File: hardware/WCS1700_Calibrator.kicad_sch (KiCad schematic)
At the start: 78 parts, among them J1 PJ-002B, J2 560020-0330, J3 282834-8, J4 Conn_01x03_Pin, J5 282834-6, Q1 AO3422, Q2 AO3422, Q3 AO3422, Q4 AO3422, Q5 AO3422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

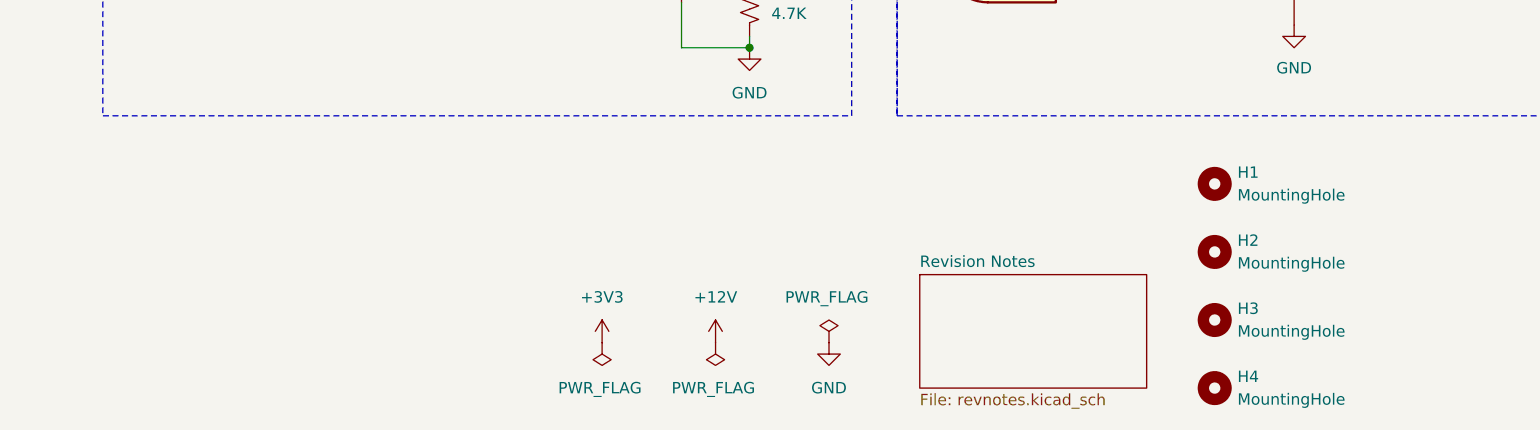
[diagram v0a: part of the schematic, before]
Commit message: Added chassis pour and tied mounting holes to it.
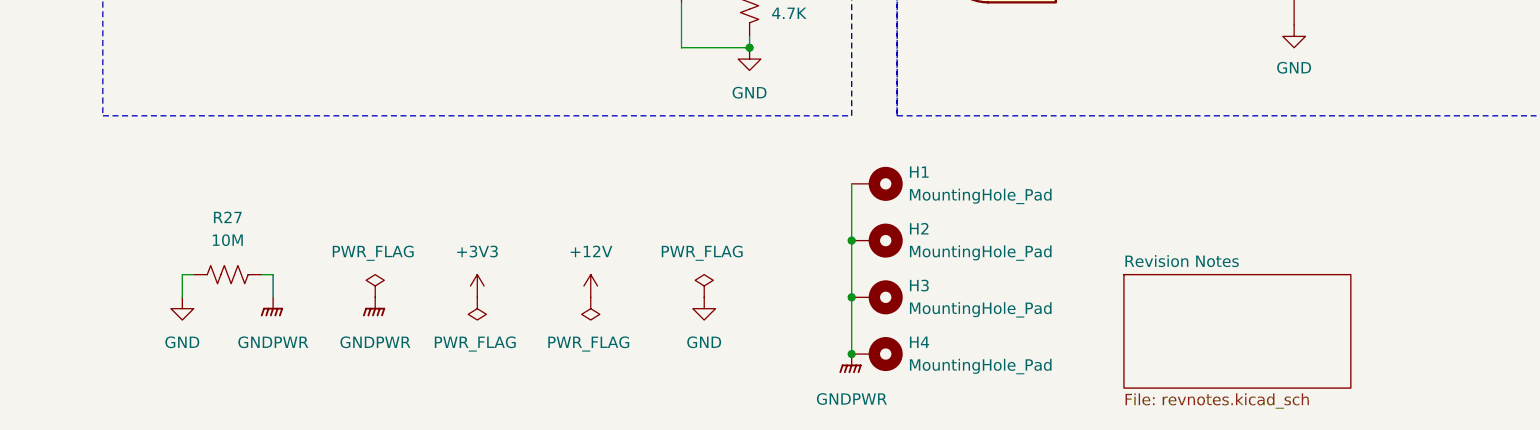
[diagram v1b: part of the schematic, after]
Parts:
- removed H1, H2, H3, H4: MountingHole, MountingHole:MountingHole_4mm_Pad_Via, symbol Mechanical:MountingHole
- added H1, H2, H3, H4: MountingHole_Pad, MountingHole:MountingHole_4mm_Pad_Via, symbol Mechanical:MountingHole_Pad
- added R27: 10M, Resistor_SMD:R_0402_1005Metric_Pad0.72x0.64mm_HandSolder, symbol Device:R_US
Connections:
- net GND: now also R27.1
- new net GNDPWR: H1.1, H2.1, H3.1, H4.1, R27.2

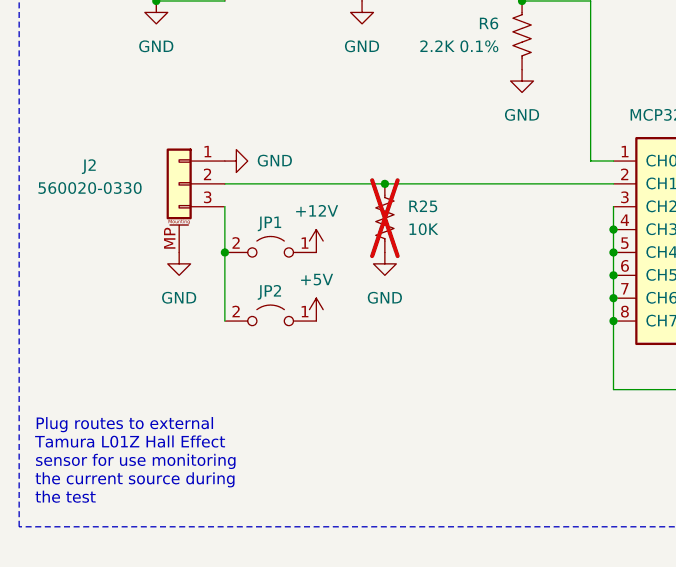
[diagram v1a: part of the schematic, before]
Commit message: Changed jumpers to resistors for L01Z sensor, updated fab/asy docs.
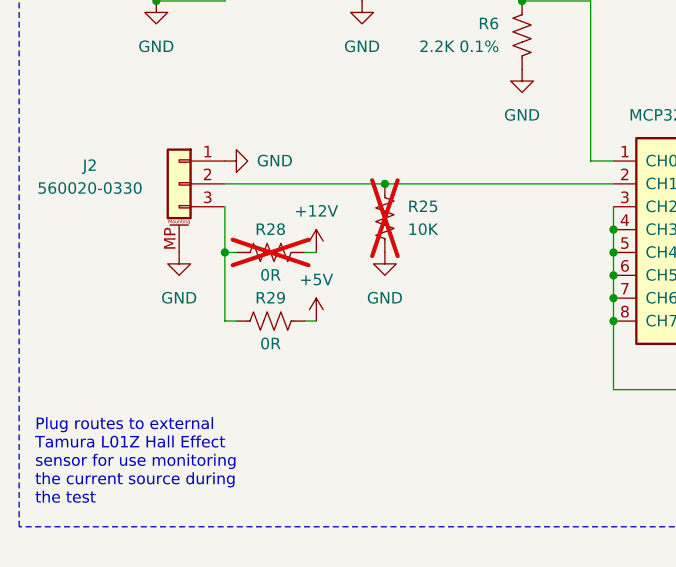
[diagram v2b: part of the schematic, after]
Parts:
- removed JP1, JP2: Jumper_2_Open, Jumper:SolderJumper-2_P1.3mm_Open_TrianglePad1.0x1.5mm, symbol Jumper:Jumper_2_Open
- added R28, R29: 0R, Resistor_SMD:R_1206_3216Metric_Pad1.30x1.75mm_HandSolder, symbol Device:R_US
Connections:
- net +12V: now also R28.2
- net +5V: now also R29.2
- net at J2.3 (Pin_3): now also R28.1, R29.1
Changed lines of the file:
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@@
   (junction (at 111.76 134.62) (diameter 0) (color 0 0 0 0)
   )
+  (junction (at 48.26 170.18) (diameter 0) (color 0 0 0 0)
+  )
   (junction (at 91.44 167.64) (diameter 0) (color 0 0 0 0)
   )
@@
   (junction (at 91.44 177.8) (diameter 0) (color 0 0 0 0)
   )
-  (junction (at 48.26 170.18) (diameter 0) (color 0 0 0 0)
-  )
   (junction (at 66.04 162.56) (diameter 0) (color 0 0 0 0)
   )
@@
     (stroke (width 0) (type default))
   )
-  (wire (pts (xy 48.26 170.18) (xy 48.26 177.8))
-    (stroke (width 0) (type default))
-  )
   (wire (pts (xy 81.28 258.064) (xy 81.28 256.54))
     (stroke (width 0) (type default))
@@
     (stroke (width 0) (type default))
   )
+  (wire (pts (xy 48.26 170.18) (xy 49.53 170.18))
+    (stroke (width 0) (type default))
+  )
   (wire (pts (xy 227.33 232.41) (xy 227.33 231.14))
     (stroke (width 0) (type default))
@@
     (stroke (width 0) (type default))
   )
+  (wire (pts (xy 57.15 170.18) (xy 58.42 170.18))
+    (stroke (width 0) (type default))
+  )
   (wire (pts (xy 351.79 152.4) (xy 355.6 152.4))
     (stroke (width 0) (type default))
@@
     (stroke (width 0) (type dash))
   )
+  (wire (pts (xy 57.15 177.8) (xy 58.42 177.8))
+    (stroke (width 0) (type default))
+  )
   (bus (pts (xy 157.48 58.42) (xy 144.78 58.42))
     (stroke (width 0) (type default))
@@
     (stroke (width 0) (type default))
   )
+  (wire (pts (xy 48.26 170.18) (xy 48.26 177.8))
+    (stroke (width 0) (type default))
+  )
   (wire (pts (xy 200.66 76.2) (xy 233.68 76.2))
     (stroke (width 0) (type default))
@@
     (stroke (width 0) (type default))
   )
+  (wire (pts (xy 48.26 177.8) (xy 49.53 177.8))
+    (stroke (width 0) (type default))
+  )
   (wire (pts (xy 88.9 160.02) (xy 91.44 160.02))
     (stroke (width 0) (type default))
@@
     )
   )
-  (symbol (lib_id "Jumper:Jumper_2_Open") (at 53.34 177.8 0) (mirror y) (unit 1)
-    (in_bom yes) (on_board yes) (dnp no)
-    (property "Reference" "JP2" (at 53.34 174.498 0)
-      (effects (font (size 1.27 1.27)))
-    )
-    (property "Value" "Jumper_2_Open" (at 53.34 173.99 0)
-      (effects (font (size 1.27 1.27)) hide)
-    )
-    (property "Footprint" "Jumper:SolderJumper-2_P1.3mm_Open_TrianglePad1.0x1.5mm" (at 53.34 177.8 0)
-      (effects (font (size 1.27 1.27)) hide)
-    )
-    (property "Datasheet" "~" (at 53.34 177.8 0)
-      (effects (font (size 1.27 1.27)) hide)
-    )
-    (pin "1")
-    (pin "2")
-    (instances
-      (project "WCS1700_Calibrator"
-        (path "/1f03928c-0f24-4718-b1ed-d2ed2f2fbec7"
-          (reference "JP2") (unit 1)
-        )
-      )
-    )
-  )
   (symbol (lib_id "power:+5V") (at 351.79 152.4 0) (unit 1)
     (in_bom yes) (on_board yes) (dnp no) (fields_autoplaced)
@@
     )
   )
-  (symbol (lib_id "Jumper:Jumper_2_Open") (at 53.34 170.18 0) (mirror y) (unit 1)
-    (in_bom yes) (on_board yes) (dnp no)
-    (property "Reference" "JP1" (at 53.34 166.878 0)
-      (effects (font (size 1.27 1.27)))
-    )
-    (property "Value" "Jumper_2_Open" (at 53.34 166.37 0)
-      (effects (font (size 1.27 1.27)) hide)
-    )
-    (property "Footprint" "Jumper:SolderJumper-2_P1.3mm_Open_TrianglePad1.0x1.5mm" (at 53.34 170.18 0)
-      (effects (font (size 1.27 1.27)) hide)
-    )
-    (property "Datasheet" "~" (at 53.34 170.18 0)
-      (effects (font (size 1.27 1.27)) hide)
-    )
-    (pin "1")
-    (pin "2")
-    (instances
-      (project "WCS1700_Calibrator"
-        (path "/1f03928c-0f24-4718-b1ed-d2ed2f2fbec7"
-          (reference "JP1") (unit 1)
-        )
-      )
-    )
-  )
   (symbol (lib_id "power:+5V") (at 215.9 190.5 0) (mirror y) (unit 1)
     (in_bom yes) (on_board yes) (dnp no) (fields_autoplaced)
@@
     )
   )
+  (symbol (lib_id "Device:R_US") (at 53.34 177.8 90) (unit 1)
+    (in_bom yes) (on_board yes) (dnp no)
+    (property "Reference" "R29" (at 53.34 175.26 90)
+      (effects (font (size 1.27 1.27)))
+    )
+    (property "Value" "0R" (at 53.34 180.34 90)
+      (effects (font (size 1.27 1.27)))
+    )
+    (property "Footprint" "Resistor_SMD:R_1206_3216Metric_Pad1.30x1.75mm_HandSolder" (at 53.594 176.784 90)
+      (effects (font (size 1.27 1.27)) hide)
+    )
+    (property "Datasheet" "~" (at 53.34 177.8 0)
+      (effects (font (size 1.27 1.27)) hide)
+    )
+    (pin "2")
+    (pin "1")
+    (instances
+      (project "WCS1700_Calibrator"
+        (path "/1f03928c-0f24-4718-b1ed-d2ed2f2fbec7"
+          (reference "R29") (unit 1)
+        )
+      )
+    )
+  )
   (symbol (lib_id "power:+3V3") (at 209.55 53.34 0) (unit 1)
     (in_bom yes) (on_board yes) (dnp no)
@@
         )
       )
+    )
+  )
+  (symbol (lib_id "Device:R_US") (at 53.34 170.18 90) (unit 1)
+    (in_bom yes) (on_board yes) (dnp yes)
+    (property "Reference" "R28" (at 53.34 167.64 90)
+      (effects (font (size 1.27 1.27)))
+    )
+    (property "Value" "0R" (at 53.34 172.72 90)
+      (effects (font (size 1.27 1.27)))
+    )
+    (property "Footprint" "Resistor_SMD:R_1206_3216Metric_Pad1.30x1.75mm_HandSolder" (at 53.594 169.164 90)
+      (effects (font (size 1.27 1.27)) hide)
+    )
+    (property "Datasheet" "~" (at 53.34 170.18 0)
+      (effects (font (size 1.27 1.27)) hide)
+    )
+    (pin "2")
+    (pin "1")
+    (instances
+      (project "WCS1700_Calibrator"
+        (path "/1f03928c-0f24-4718-b1ed-d2ed2f2fbec7"
+          (reference "R28") (unit 1)
+        )
+      )
